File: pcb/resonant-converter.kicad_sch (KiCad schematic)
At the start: 61 parts, among them J1 Banana_Jack_Keystone_575-8, J2 Banana_Jack_Keystone_575-8, J3 Banana_Jack_Keystone_575-8, J4 Banana_Jack_Keystone_575-8, J6 Molex_KK_1x4_0470531000, Q1 MDU04N010VRH, Q2 MDU04N010VRH, Q3 HSU30N20, Q4 HSU30N20, T1 B66206W1110T001, U1 UCC256610DDBR, U2 TEA2096T/1J, U4 PC817X2CSP9F, U5 TL431AIDBVR

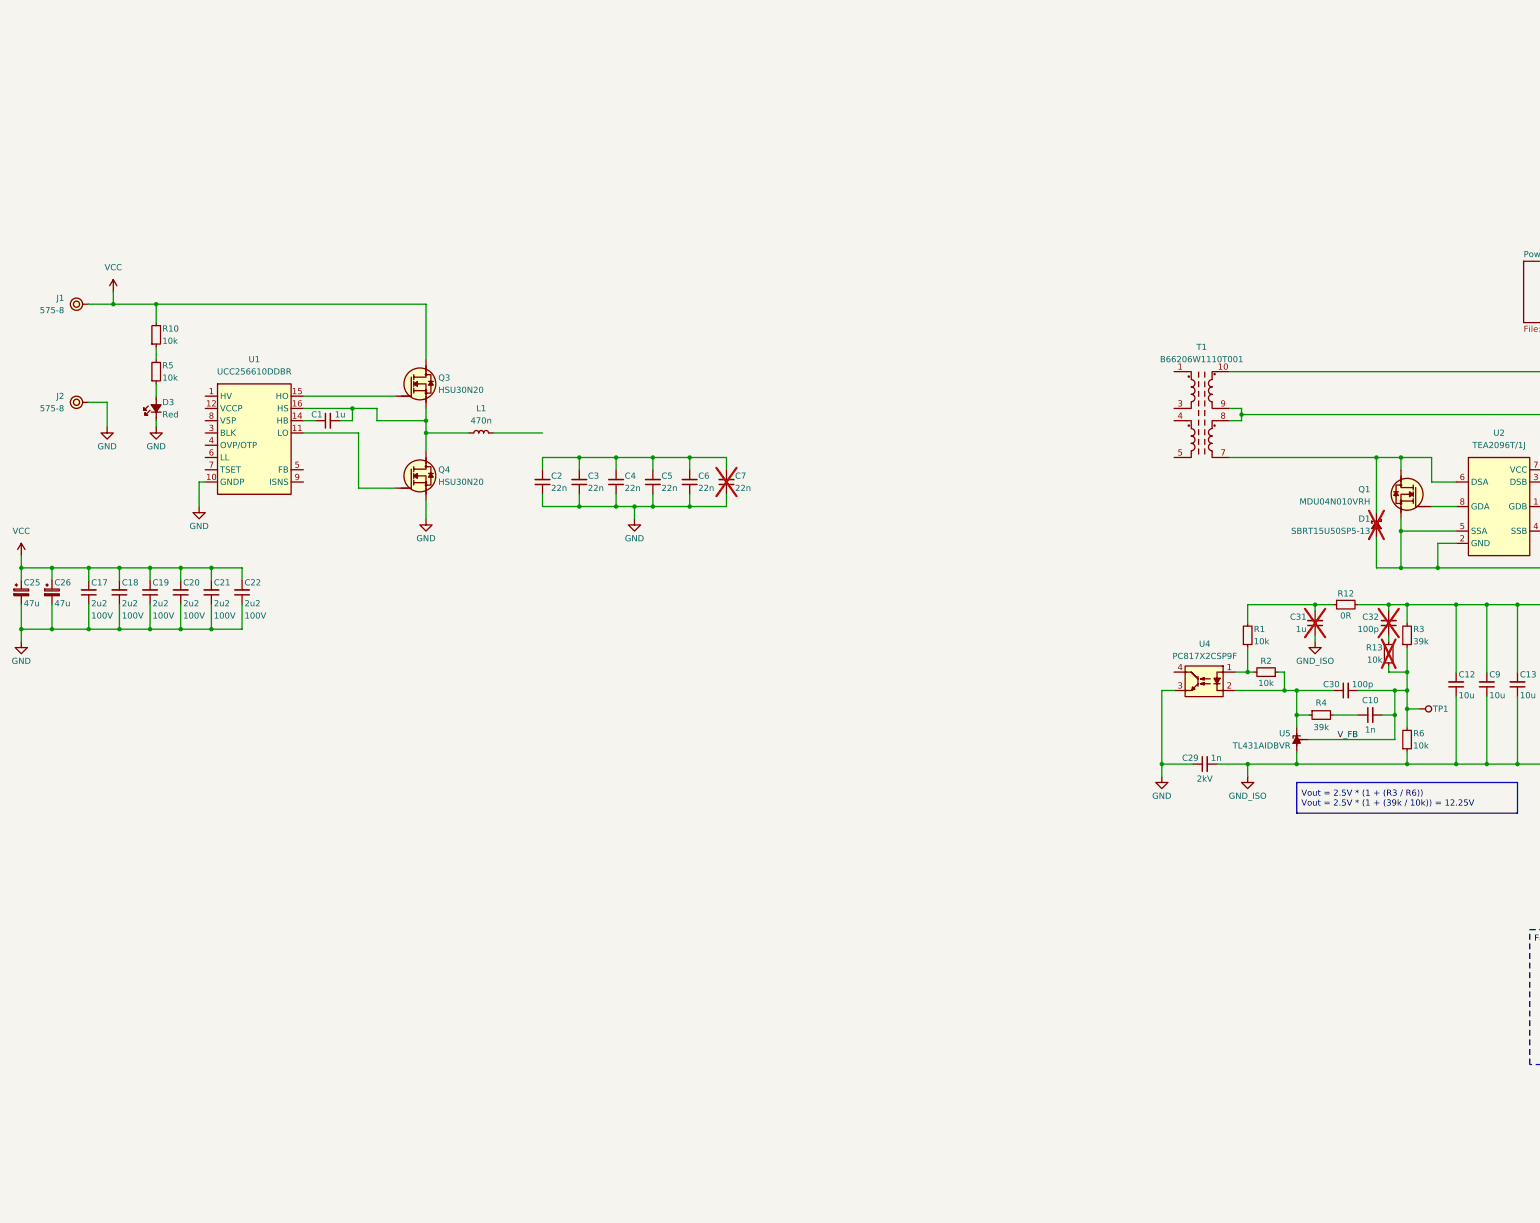
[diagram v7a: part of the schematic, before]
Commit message: [#3] Complete primary side schematic
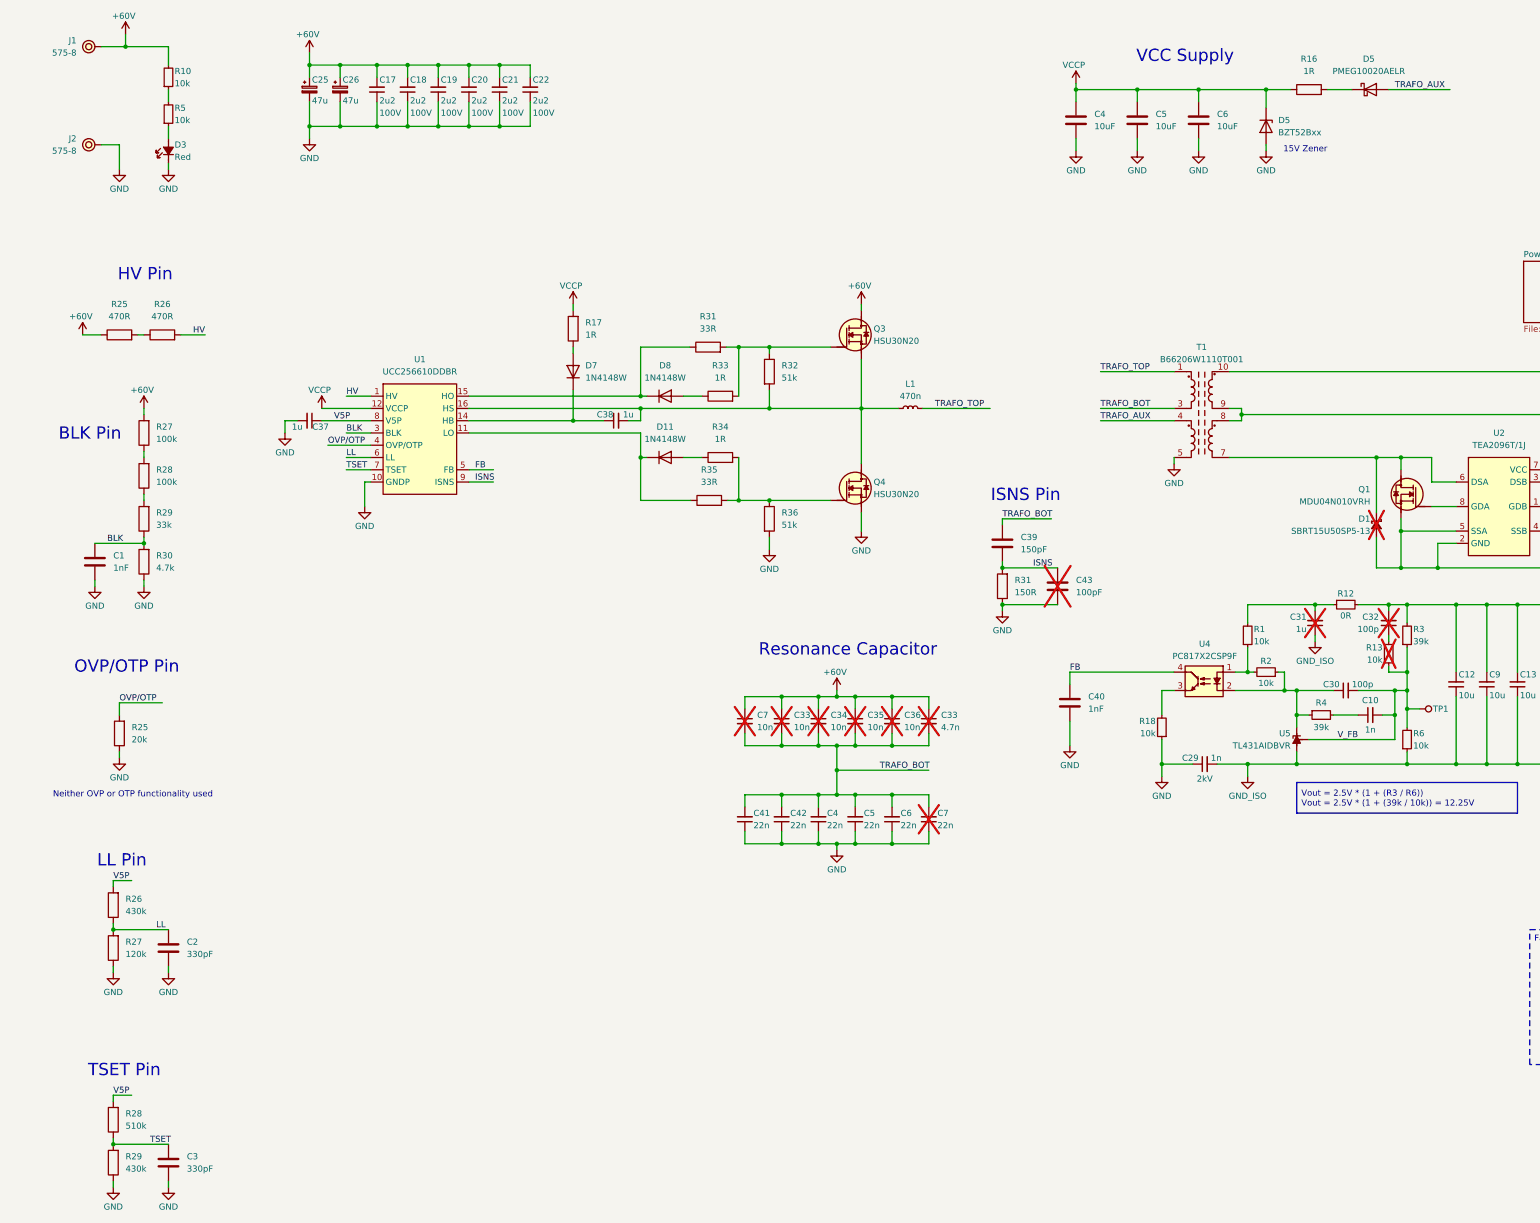
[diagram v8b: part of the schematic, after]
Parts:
- removed C1: C-1u-0402, DW-footprints:C_0402_1005Metric, symbol DW-capacitors:C-1u-0402
- removed C2, C3: C-22n-100V-C0G-1206, DW-footprints:C_1206_3216Metric, symbol DW-capacitors:C-22n-100V-C0G-1206
- added C1, C40: 1nF, Capacitor_SMD:C_0402_1005Metric, symbol Device:C
- added C2, C3: 330pF, symbol Device:C
- added C33: 4.7n, Capacitor_SMD:C_1206_3216Metric, symbol Device:C_Small
- added C33, C34, C35, C36, C7: 10n, Capacitor_SMD:C_1206_3216Metric, symbol Device:C_Small
- added C37, C38: C-1u-0402, DW-footprints:C_0402_1005Metric, symbol DW-capacitors:C-1u-0402
- added C39: 150pF, Capacitor_SMD:C_1206_3216Metric, symbol Device:C
- added C4, C5, C6: 10uF, Capacitor_SMD:C_0805_2012Metric, symbol Device:C
- added C41, C42: C-22n-100V-C0G-1206, DW-footprints:C_1206_3216Metric, symbol DW-capacitors:C-22n-100V-C0G-1206
- added C43: 100pF, Capacitor_SMD:C_0402_1005Metric, symbol Device:C
- added D11, D7, D8: 1N4148W, Diode_SMD:D_SOD-123, symbol Diode:1N4148W
- added D5: BZT52Bxx, Diode_SMD:D_SOD-123F, symbol Diode:BZT52Bxx
- added D5: PMEG10020AELR, Diode_SMD:Nexperia_CFP3_SOD-123W, symbol Diode:PMEG10020AELR
- added R16: 1R, Resistor_SMD:R_1206_3216Metric, symbol Device:R
- added R17, R33, R34: 1R, Resistor_SMD:R_0402_1005Metric, symbol Device:R
- added R18: R-10k-0402, DW-footprints:R_0402_1005Metric, symbol DW-resistors:R-10k-0402
- added R25: 20k, Resistor_SMD:R_0402_1005Metric, symbol Device:R
- added R25, R26: 470R, Resistor_SMD:R_0402_1005Metric, symbol Device:R
- added R26, R29: 430k, Resistor_SMD:R_0402_1005Metric, symbol Device:R
- added R27, R28: 100k, Resistor_SMD:R_0402_1005Metric, symbol Device:R
- added R27: 120k, Resistor_SMD:R_0402_1005Metric, symbol Device:R
- added R28: 510k, Resistor_SMD:R_0402_1005Metric, symbol Device:R
- added R29: 33k, Resistor_SMD:R_0402_1005Metric, symbol Device:R
- added R30: 4.7k, Resistor_SMD:R_0402_1005Metric, symbol Device:R
- added R31: 150R, Resistor_SMD:R_0402_1005Metric, symbol Device:R
- added R31, R35: 33R, Resistor_SMD:R_0402_1005Metric, symbol Device:R
- added R32, R36: 51k, Resistor_SMD:R_0402_1005Metric, symbol Device:R
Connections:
- net GND: now also T1.5, C1.2, C2.2, C3.2, C37.2, C4.2, C40.2, C41.1, C42.1, C43.2, C5.2, C6.2, D5.2 (A), R18.1, R25.1, R27.1, R29.1, R30.1, R31.1, R36.2; no longer U4.3
- net at U1.15 (HO): now also D8.1 (K), R31.1; no longer Q3.1 (G)
- net at L1.1, Q3.2 (S), Q4.3 (D)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: now also C38.2, R32.2
- net TRAFO_BOT: now reaches C4.2, C5.2, C6.2, C7.2
- net TRAFO_BOT: now also T1.3, C33.2, C33.2, C34.2, C35.2, C36.2, C39.1, C41.2, C42.2, C7.2
- net HV: now reaches U1.1 (HV)
- net HV: now also R26.2
- net at U1.11 (LO): now also D11.1 (K), R35.1; no longer Q4.1 (G)
- net VCCP: now reaches U1.12 (VCCP)
- net VCCP: now also C4.1, C5.1, C6.1, D5.1 (K), R16.1, R17.2
- net at U1.14 (HB): now also C38.1, D7.1 (K)
- net BLK: now reaches U1.3 (BLK)
- net BLK: now also C1.1, R29.1, R30.2
- net OVP/OTP: now reaches U1.4 (OVP/OTP)
- net OVP/OTP: now also R25.2
- net FB: now reaches U1.5 (FB)
- net FB: now also U4.4, C40.1
- net LL: now reaches U1.6 (LL)
- net LL: now also C2.1, R26.1, R27.2
- net TSET: now reaches U1.7 (TSET)
- net TSET: now also C3.1, R28.1, R29.2
- net V5P: now reaches U1.8 (V5P)
- net V5P: now also C37.1, R26.2, R28.2
- net ISNS: now reaches U1.9 (ISNS)
- net ISNS: now also C39.2, C43.1, R31.2
- net TRAFO_TOP: now reaches L1.2
- net TRAFO_TOP: now also T1.1
- net TRAFO_AUX: now reaches T1.4
- net TRAFO_AUX: now also D5.2 (A)
- net VCC renamed +60V
- net +60V: now also C33.1, C33.1, C34.1, C35.1, C36.1, C7.1, R25.1, R27.2
- new net: D8.2 (A), R33.1
- new net: R18.2, U4.3
- new net: D7.2 (A), R17.1
- new net: R25.2, R26.1
- new net: Q3.1 (G), R31.2, R32.1, R33.2
- new net: D5.1 (K), R16.2
- new net: D11.2 (A), R34.1
- new net: R28.1, R29.2
- new net: R27.1, R28.2
- new net: Q4.1 (G), R34.2, R35.2, R36.1
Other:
- note added: "15V Zener"
- note added: "BLK Pin"
- note added: "HV Pin"
- note added: "ISNS Pin"
- note added: "LL Pin"
- note added: "Neither OVP or OTP functionality used"
- note added: "OVP/OTP Pin"
- note added: "Resonance Capacitor"
- note added: "TSET Pin"
- note added: "VCC Supply"
- moved on the sheet: C17, C18, C19, C20, C21, C22, C25, C26, C4, C5, C6, C7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
